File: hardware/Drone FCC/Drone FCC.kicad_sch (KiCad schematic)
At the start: 6 parts, among them J21 Micro_SD_Card_Det_Hirose_DM3AT, J23 47589-0001

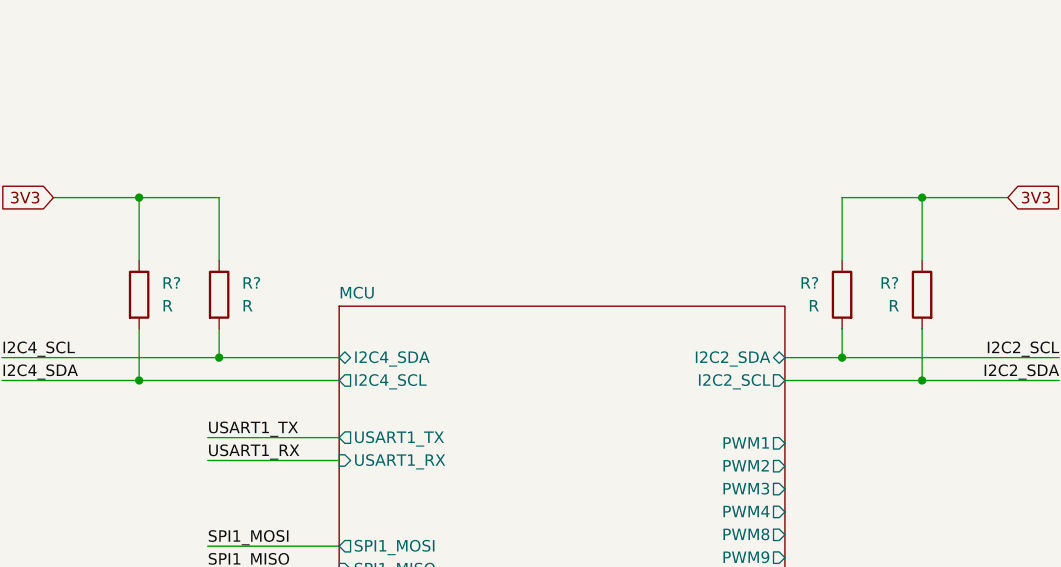
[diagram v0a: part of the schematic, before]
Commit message: changed mag connector for GPS module DF-13
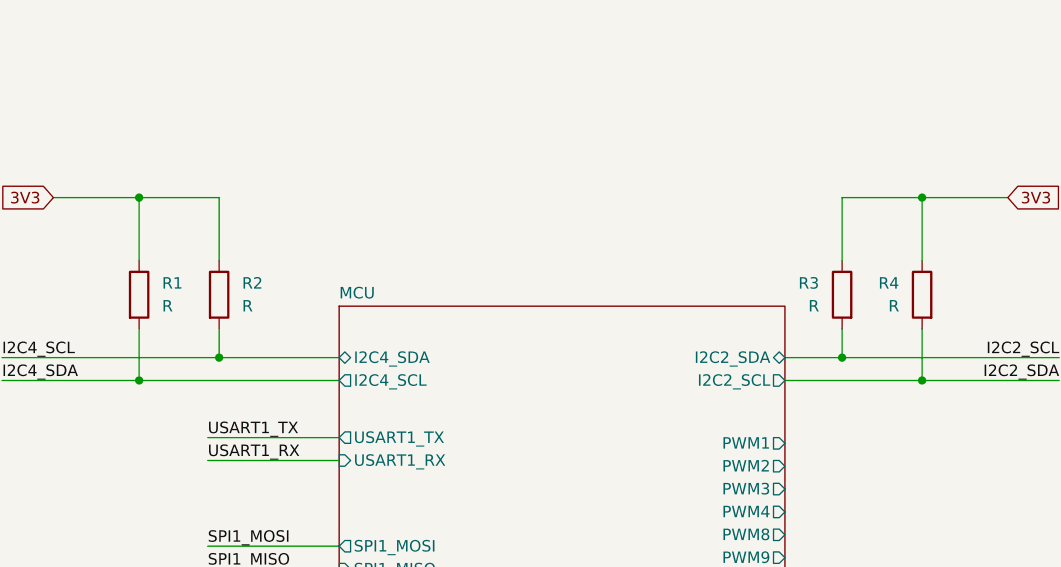
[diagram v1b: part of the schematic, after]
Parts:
- gave numbers to parts that had none: 4
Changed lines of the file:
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@@
   (symbol (lib_id "Device:R") (at 152.4 48.895 0) (unit 1)
     (in_bom yes) (on_board yes) (fields_autoplaced)
-    (property "Reference" "R?" (id 0) (at 154.94 47.6249 0)
+    (property "Reference" "R2" (id 0) (at 154.94 47.6249 0)
       (effects (font (size 1.27 1.27)) (justify left))
     )
@@
   (symbol (lib_id "Device:R") (at 143.51 48.895 0) (unit 1)
     (in_bom yes) (on_board yes) (fields_autoplaced)
-    (property "Reference" "R?" (id 0) (at 146.05 47.6249 0)
+    (property "Reference" "R1" (id 0) (at 146.05 47.6249 0)
       (effects (font (size 1.27 1.27)) (justify left))
     )
@@
   (symbol (lib_id "Device:R") (at 221.615 48.895 0) (mirror y) (unit 1)
     (in_bom yes) (on_board yes) (fields_autoplaced)
-    (property "Reference" "R?" (id 0) (at 219.075 47.6249 0)
+    (property "Reference" "R3" (id 0) (at 219.075 47.6249 0)
       (effects (font (size 1.27 1.27)) (justify left))
     )
@@
   (symbol (lib_id "Device:R") (at 230.505 48.895 0) (mirror y) (unit 1)
     (in_bom yes) (on_board yes) (fields_autoplaced)
-    (property "Reference" "R?" (id 0) (at 227.965 47.6249 0)
+    (property "Reference" "R4" (id 0) (at 227.965 47.6249 0)
       (effects (font (size 1.27 1.27)) (justify left))
     )
@@
       (reference "#PWR0115") (unit 1) (value "GND") (footprint "")
     )
-    (path "/2dea4649-a03b-4105-a448-fdfd58cb624b/60b3591a-d940-4800-a3ad-e92d28979532"
+    (path "/2dea4649-a03b-4105-a448-fdfd58cb624b/cea69c83-349e-491b-9e3c-64f53b0a2bd7"
       (reference "#PWR0116") (unit 1) (value "GND") (footprint "")
     )
@@
     )
     (path "/2dea4649-a03b-4105-a448-fdfd58cb624b/1ada52bf-3160-4b2e-8e93-ed65b64dff92"
-      (reference "J1") (unit 1) (value "Dupont 2 filas x 3 pines") (footprint "Connector_PinHeader_2.54mm:PinHeader_2x03_P2.54mm_Horizontal")
+      (reference "J1") (unit 1) (value "Mag Dupont") (footprint "Connector_PinHeader_2.54mm:PinHeader_2x03_P2.54mm_Horizontal")
     )
     (path "/2dea4649-a03b-4105-a448-fdfd58cb624b/b079b46a-f7fc-473d-a5cf-a695656f1e39"
-      (reference "J2") (unit 1) (value "Conector GPS Auxiliar Dupont") (footprint "Connector_PinHeader_2.54mm:PinHeader_2x03_P2.54mm_Horizontal")
+      (reference "J2") (unit 1) (value "GPS Dupont") (footprint "Connector_PinHeader_2.54mm:PinHeader_2x03_P2.54mm_Horizontal")
     )
     (path "/dd9839f2-48a6-46c9-b84f-4c2c3431def5/2c0e7e5c-a396-43ba-a674-e23b0aa3ed8c"
@@
     )
     (path "/2dea4649-a03b-4105-a448-fdfd58cb624b/b2d2d786-d830-41a8-86bc-a5ceb742f967"
-      (reference "J19") (unit 1) (value "GPS M8N") (footprint "Connector_Hirose:Hirose_DF13C_CL535-0406-3-51_1x06-1MP_P1.25mm_Vertical")
-    )
-    (path "/2dea4649-a03b-4105-a448-fdfd58cb624b/06952a31-81b8-47ac-a344-8aaff0a89059"
-      (reference "J20") (unit 1) (value "Conector Magnetómetro I2C DF13") (footprint "Connector_Hirose:Hirose_DF13C_CL535-0406-3-51_1x06-1MP_P1.25mm_Vertical")
+      (reference "J19") (unit 1) (value "GPS M8N - DF13") (footprint "Connector_Hirose:Hirose_DF13C_CL535-0406-3-51_1x06-1MP_P1.25mm_Vertical")
+    )
+    (path "/2dea4649-a03b-4105-a448-fdfd58cb624b/2f78d477-9a33-45b7-b681-4c853f159a72"
+      (reference "J20") (unit 1) (value "Mag DF13") (footprint "Connector_Hirose:Hirose_DF13C_CL535-0404-8-51_1x04-1MP_P1.25mm_Vertical")
     )
     (path "/9d87abcb-f095-4bbc-8a62-a00271c99c74"
@@
       (reference "J28") (unit 1) (value "Conn_01x06") (footprint "Connector_Hirose:Hirose_DF13C_CL535-0406-3-51_1x06-1MP_P1.25mm_Vertical")
     )
+    (path "/9bc65728-e237-4f6c-82eb-0920dd4372d2"
+      (reference "R1") (unit 1) (value "R") (footprint "")
+    )
     (path "/23eb84d1-346d-494f-a7a3-f17e51c94eb4"
-      (reference "R?") (unit 1) (value "R") (footprint "")
-    )
-    (path "/9bc65728-e237-4f6c-82eb-0920dd4372d2"
-      (reference "R?") (unit 1) (value "R") (footprint "")
+      (reference "R2") (unit 1) (value "R") (footprint "")
     )
     (path "/bf56a9a0-87b8-4975-8c8a-f06525b46212"
-      (reference "R?") (unit 1) (value "R") (footprint "")
+      (reference "R3") (unit 1) (value "R") (footprint "")
     )
     (path "/ec16aef2-cd03-4558-8bbc-13cfd44062fb"
-      (reference "R?") (unit 1) (value "R") (footprint "")
+      (reference "R4") (unit 1) (value "R") (footprint "")
     )
     (path "/2dea4649-a03b-4105-a448-fdfd58cb624b/526c1ffa-b5c3-4a19-b2e6-f432001e1abc"
@@
       (reference "U2") (unit 1) (value "ILPS22QSTR") (footprint "ILPS22QSTR:ILPS22QSTR")
     )
+    (path "/7aefb805-1ee8-4c99-a02a-c3e1e1ca7ccb/90b6111d-e183-4fd3-9c15-536660e047e9"
+      (reference "U3") (unit 1) (value "STM32F746ZGTx") (footprint "Package_QFP:LQFP-144_20x20mm_P0.5mm")
+    )
     (path "/f05f239e-e978-4f7d-94d0-b7e31d2fe727/0976ceae-974b-4c9d-9c30-da4f63145ad3"
       (reference "U4") (unit 1) (value "SN65HVD230") (footprint "Package_SO:SOIC-8_3.9x4.9mm_P1.27mm")
@@
       (reference "U5") (unit 1) (value "SN65HVD230") (footprint "Package_SO:SOIC-8_3.9x4.9mm_P1.27mm")
     )
-    (path "/7aefb805-1ee8-4c99-a02a-c3e1e1ca7ccb/90b6111d-e183-4fd3-9c15-536660e047e9"
-      (reference "U?") (unit 1) (value "STM32F746ZGTx") (footprint "Package_QFP:LQFP-144_20x20mm_P0.5mm")
-    )
-  )
+  )

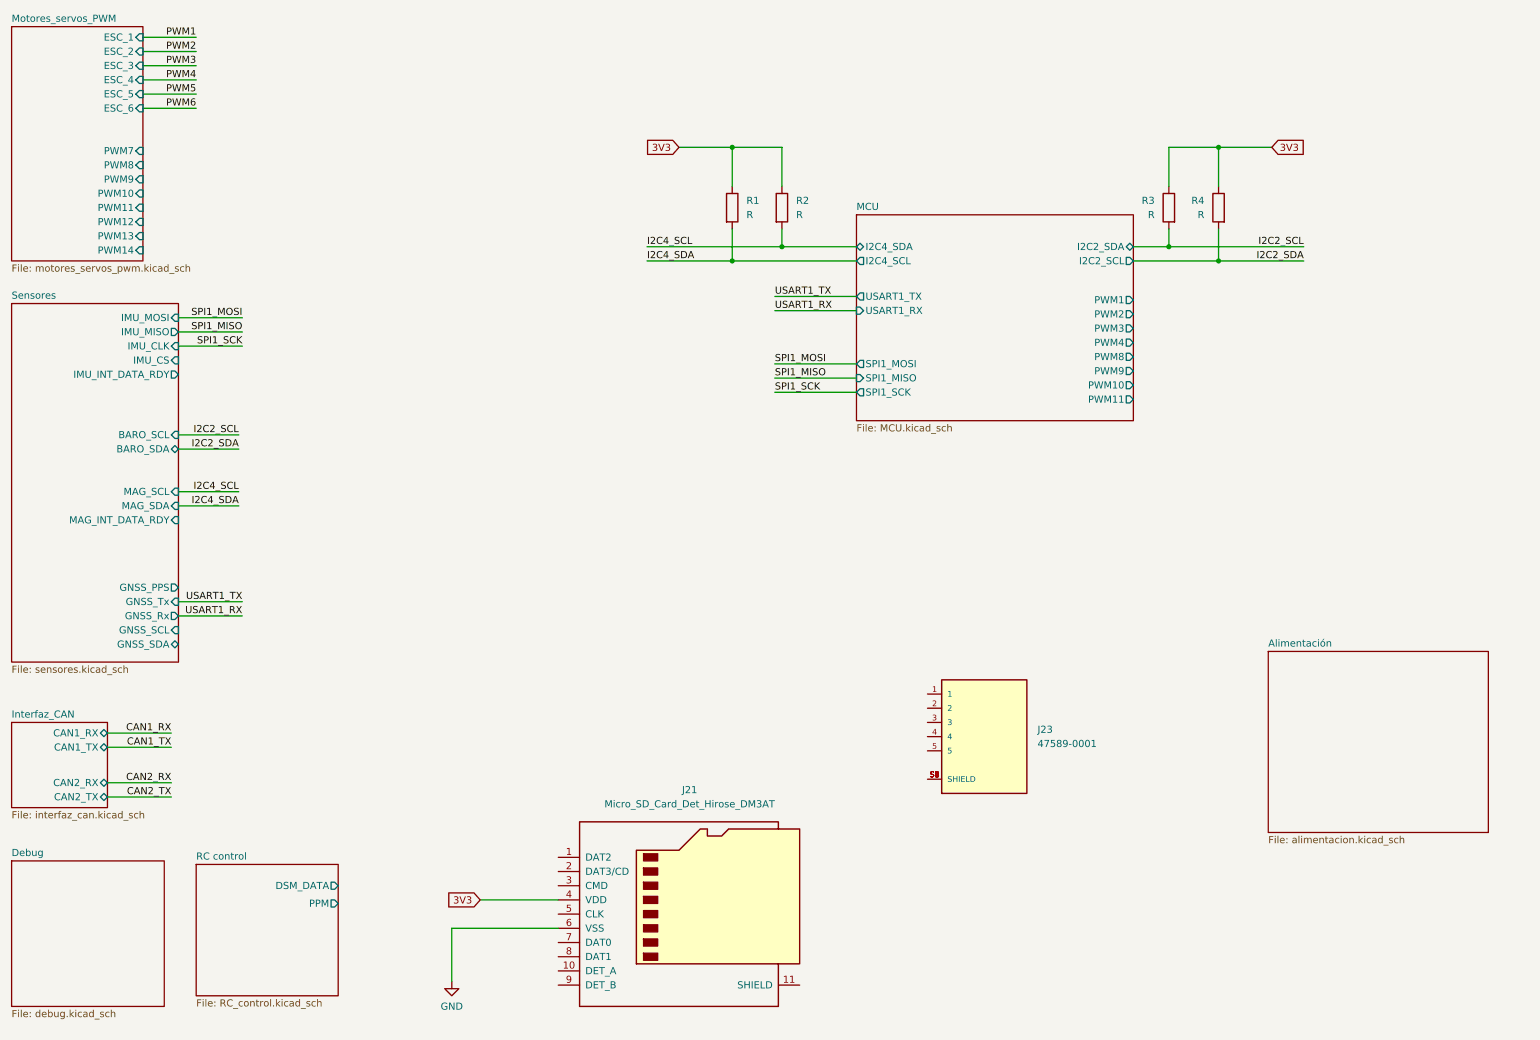
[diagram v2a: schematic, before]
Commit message: add functional schematic for microSD
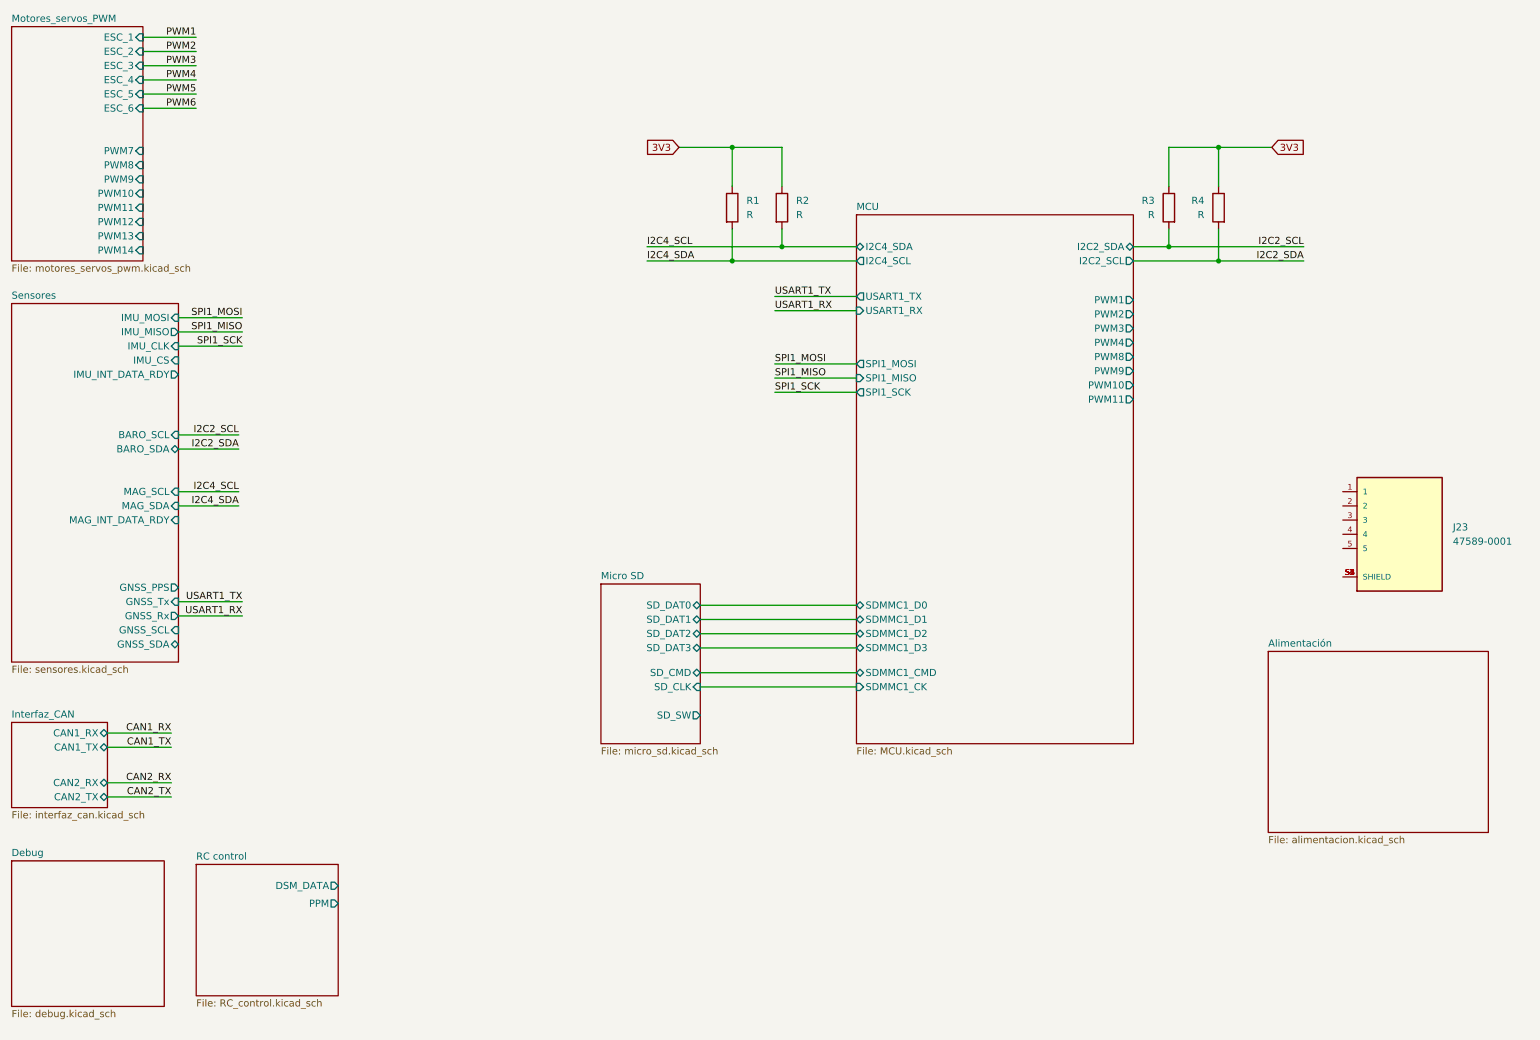
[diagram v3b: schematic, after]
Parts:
- removed J21: Micro_SD_Card_Det_Hirose_DM3AT, DM3AT-SF-PEJM5:HRS_DM3AT-SF-PEJM5, symbol Connector:Micro_SD_Card_Det_Hirose_DM3AT
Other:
- added sheet Micro SD (micro_sd.kicad_sch)
- sheet MCU ports: added SDMMC1_CK, SDMMC1_CMD, SDMMC1_D0, SDMMC1_D1, SDMMC1_D2, SDMMC1_D3; removed none
- moved on the sheet: J23

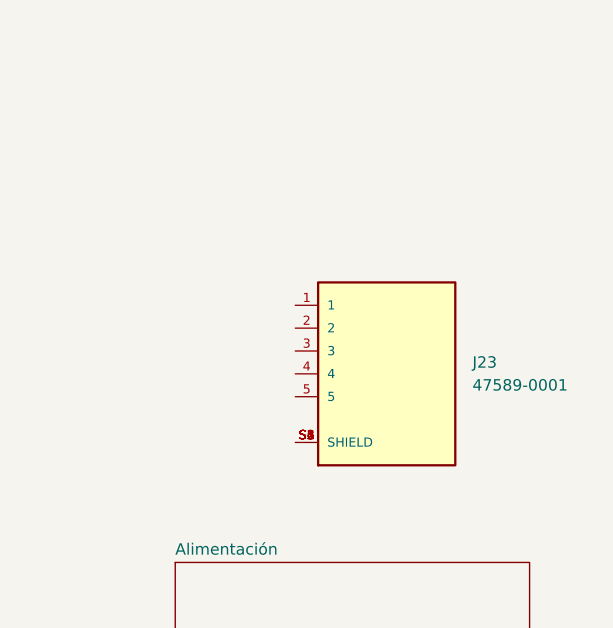
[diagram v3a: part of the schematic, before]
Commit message: changed usb 2.0 AB connector for usb 2.0 B
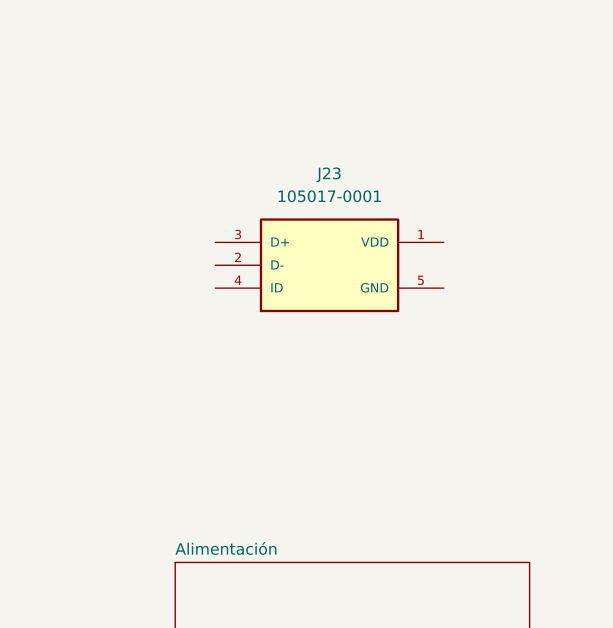
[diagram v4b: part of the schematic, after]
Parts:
- removed J23: 47589-0001, 47589-0001:MOLEX_47589-0001, symbol 47589-0001:47589-0001
- added J23: 105017-0001, 105017-0001:MOLEX_105017-0001, symbol 105017-0001:105017-0001
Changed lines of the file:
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@@
     (pin "2")
   )
-  (symbol (lib_id "47589-0001:47589-0001") (at 262.89 107.315 0) (unit 1)
+  (symbol (lib_id "Device:R") (at 143.51 48.895 0) (unit 1)
     (in_bom yes) (on_board yes) (fields_autoplaced)
-    (property "Reference" "J23" (id 0) (at 272.415 106.0449 0)
-      (effects (font (size 1.27 1.27)) (justify left))
-    )
-    (property "Value" "47589-0001" (id 1) (at 272.415 108.5849 0)
-      (effects (font (size 1.27 1.27)) (justify left))
-    )
-    (property "Footprint" "47589-0001:MOLEX_47589-0001" (id 2) (at 262.89 107.315 0)
+    (property "Reference" "R1" (id 0) (at 146.05 47.6249 0)
+      (effects (font (size 1.27 1.27)) (justify left))
+    )
+    (property "Value" "R" (id 1) (at 146.05 50.1649 0)
+      (effects (font (size 1.27 1.27)) (justify left))
+    )
+    (property "Footprint" "" (id 2) (at 141.732 48.895 90)
+      (effects (font (size 1.27 1.27)) hide)
+    )
+    (property "Datasheet" "~" (id 3) (at 143.51 48.895 0)
+      (effects (font (size 1.27 1.27)) hide)
+    )
+    (pin "1")
+    (pin "2")
+  )
+  (symbol (lib_id "105017-0001:105017-0001") (at 256.54 95.25 0) (unit 1)
+    (in_bom yes) (on_board yes) (fields_autoplaced)
+    (property "Reference" "J23" (id 0) (at 256.54 85.09 0))
+    (property "Value" "105017-0001" (id 1) (at 256.54 87.63 0))
+    (property "Footprint" "105017-0001:MOLEX_105017-0001" (id 2) (at 256.54 95.25 0)
       (effects (font (size 1.27 1.27)) (justify bottom) hide)
     )
-    (property "Datasheet" "" (id 3) (at 262.89 107.315 0)
-      (effects (font (size 1.27 1.27)) hide)
-    )
-    (property "MF" "Molex" (id 4) (at 262.89 107.315 0)
-      (effects (font (size 1.27 1.27)) (justify bottom) hide)
-    )
-    (property "PARTREV" "E" (id 5) (at 262.89 107.315 0)
-      (effects (font (size 1.27 1.27)) (justify bottom) hide)
-    )
-    (property "STANDARD" "Manufacturer Recommendations" (id 6) (at 262.89 107.315 0)
-      (effects (font (size 1.27 1.27)) (justify bottom) hide)
+    (property "Datasheet" "" (id 3) (at 256.54 95.25 0)
+      (effects (font (size 1.27 1.27)) hide)
     )
     (pin "1")
@@
     (pin "4")
     (pin "5")
-    (pin "S1")
-    (pin "S2")
-    (pin "S3")
-    (pin "S4")
-    (pin "S5")
-    (pin "S6")
-  )
-  (symbol (lib_id "Device:R") (at 143.51 48.895 0) (unit 1)
-    (in_bom yes) (on_board yes) (fields_autoplaced)
-    (property "Reference" "R1" (id 0) (at 146.05 47.6249 0)
-      (effects (font (size 1.27 1.27)) (justify left))
-    )
-    (property "Value" "R" (id 1) (at 146.05 50.1649 0)
-      (effects (font (size 1.27 1.27)) (justify left))
-    )
-    (property "Footprint" "" (id 2) (at 141.732 48.895 90)
-      (effects (font (size 1.27 1.27)) hide)
-    )
-    (property "Datasheet" "~" (id 3) (at 143.51 48.895 0)
-      (effects (font (size 1.27 1.27)) hide)
-    )
-    (pin "1")
-    (pin "2")
   )
   (symbol (lib_id "Device:R") (at 221.615 48.895 0) (mirror y) (unit 1)
@@
       (reference "#PWR0116") (unit 1) (value "GND") (footprint "")
     )
+    (path "/69dfc791-495c-4b9c-b2fd-05bf30e46c19/f7183e1c-f767-4db8-a001-f7ecc7f212f8"
+      (reference "#PWR0117") (unit 1) (value "GND") (footprint "")
+    )
     (path "/79e0599a-7098-4a96-b5a2-c7f60ed6c34f/60d2136a-a5f2-46f4-98c8-e7f4034c2594"
       (reference "#PWR0118") (unit 1) (value "GND") (footprint "")
@@
       (reference "#PWR0121") (unit 1) (value "GND") (footprint "")
     )
-    (path "/69dfc791-495c-4b9c-b2fd-05bf30e46c19/f7183e1c-f767-4db8-a001-f7ecc7f212f8"
-      (reference "#PWR?") (unit 1) (value "GND") (footprint "")
-    )
     (path "/2dea4649-a03b-4105-a448-fdfd58cb624b/7430465c-9d48-4f87-807f-b7d872f0d403"
       (reference "C1") (unit 1) (value "0.1u") (footprint "")
@@
       (reference "J22") (unit 1) (value "Conn_02x05_Odd_Even") (footprint "FTSH-105-01-F-DV-K-TR:SAMTEC_FTSH-105-01-F-DV-P-TR")
     )
-    (path "/7d272a67-6550-4537-bde4-348224765d34"
-      (reference "J23") (unit 1) (value "47589-0001") (footprint "47589-0001:MOLEX_47589-0001")
+    (path "/ad6e619b-5cad-40b7-a35a-90b6675364d9"
+      (reference "J23") (unit 1) (value "105017-0001") (footprint "105017-0001:MOLEX_105017-0001")
     )
     (path "/2e02b919-519b-4cae-a6fb-682f19bf0ab7/6299bbba-da38-4b1d-aee3-1b5562e402d2"
@@
       (reference "R4") (unit 1) (value "R") (footprint "")
     )
+    (path "/69dfc791-495c-4b9c-b2fd-05bf30e46c19/853e49c1-2cd0-4ca7-b6ee-c601f0208463"
+      (reference "R5") (unit 1) (value "10k") (footprint "")
+    )
     (path "/69dfc791-495c-4b9c-b2fd-05bf30e46c19/2915d28b-90f2-4985-90d2-baf59e87c4aa"
-      (reference "R?") (unit 1) (value "10k") (footprint "")
+      (reference "R6") (unit 1) (value "10k") (footprint "")
     )
     (path "/69dfc791-495c-4b9c-b2fd-05bf30e46c19/3bd2c5fe-4d13-48c2-a2c0-64d13c2de098"
-      (reference "R?") (unit 1) (value "10k") (footprint "")
+      (reference "R7") (unit 1) (value "10k") (footprint "")
+    )
+    (path "/69dfc791-495c-4b9c-b2fd-05bf30e46c19/bd5aecf5-9ea0-4949-a023-c36e3b35dea1"
+      (reference "R8") (unit 1) (value "10k") (footprint "")
     )
     (path "/69dfc791-495c-4b9c-b2fd-05bf30e46c19/74336402-9770-4ecf-a05e-6b3b439372ed"
-      (reference "R?") (unit 1) (value "10k") (footprint "")
-    )
-    (path "/69dfc791-495c-4b9c-b2fd-05bf30e46c19/853e49c1-2cd0-4ca7-b6ee-c601f0208463"
-      (reference "R?") (unit 1) (value "10k") (footprint "")
+      (reference "R9") (unit 1) (value "10k") (footprint "")
     )
     (path "/69dfc791-495c-4b9c-b2fd-05bf30e46c19/aceeb8de-bbce-461a-8c18-d44e79815bae"
-      (reference "R?") (unit 1) (value "10k") (footprint "")
-    )
-    (path "/69dfc791-495c-4b9c-b2fd-05bf30e46c19/bd5aecf5-9ea0-4949-a023-c36e3b35dea1"
-      (reference "R?") (unit 1) (value "10k") (footprint "")
+      (reference "R10") (unit 1) (value "10k") (footprint "")
     )
     (path "/2dea4649-a03b-4105-a448-fdfd58cb624b/526c1ffa-b5c3-4a19-b2e6-f432001e1abc"
